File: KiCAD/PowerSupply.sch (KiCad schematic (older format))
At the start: 12 parts, among them J4 USB-Micro, Q1 3.7A, 30V, U2 LM1117-5.0, U3 AP2112K-3.3

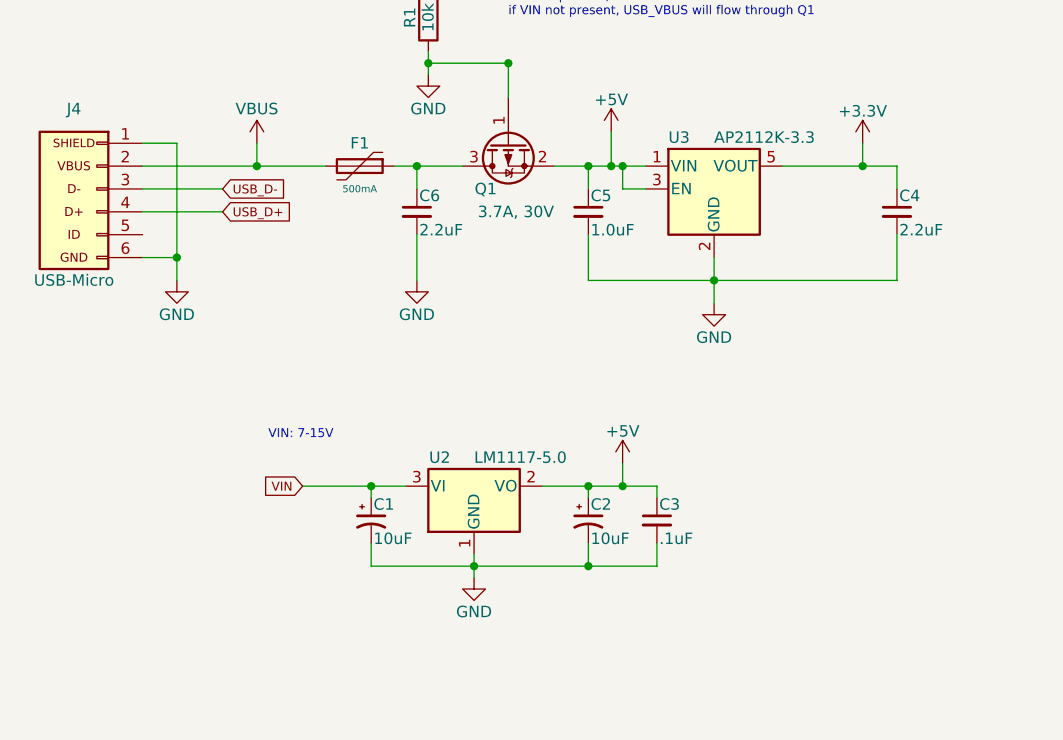
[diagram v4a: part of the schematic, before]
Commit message: Board layout and fixing schematic errors
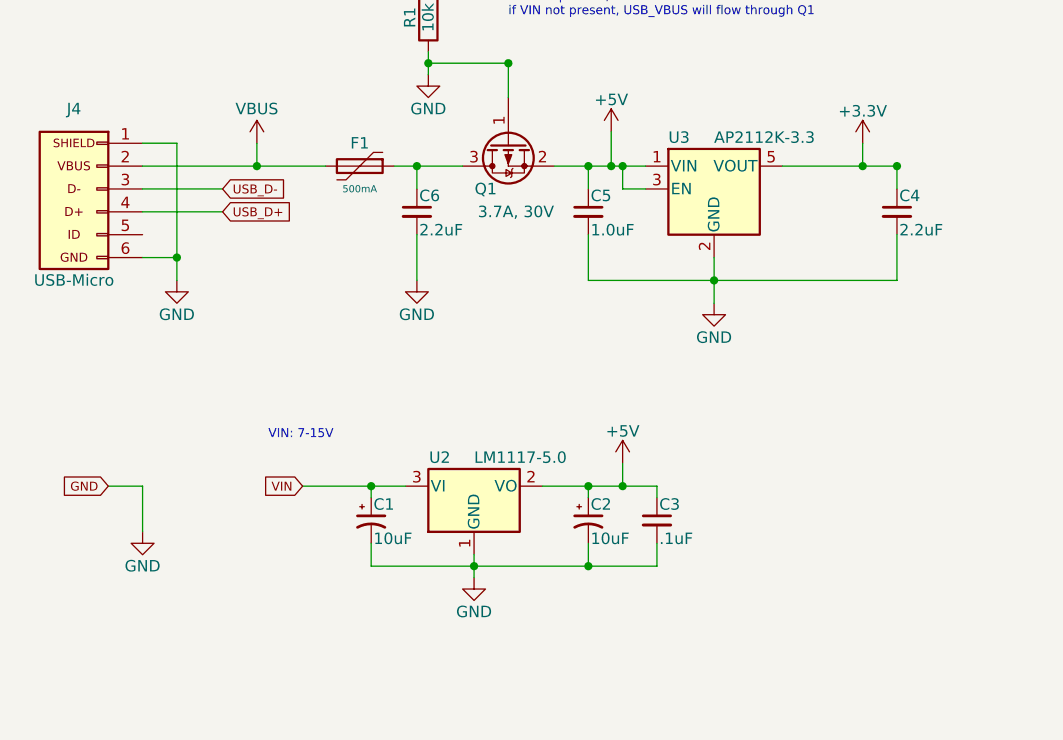
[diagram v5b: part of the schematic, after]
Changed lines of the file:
@@
 $EndDescr
 $Comp
-L GND #PWR027
+L GND #PWR025
 U 1 1 5BF271E8
 P 4600 3950
-F 0 "#PWR027" H 4600 3700 50  0001 C CNN
+F 0 "#PWR025" H 4600 3700 50  0001 C CNN
 F 1 "GND" H 4600 3800 50  0000 C CNN
 F 2 "" H 4600 3950 50  0001 C CNN
@@
 $EndComp
 $Comp
-L GND #PWR028
+L GND #PWR026
 U 1 1 5BF2720F
 P 5700 3050
-F 0 "#PWR028" H 5700 2800 50  0001 C CNN
+F 0 "#PWR026" H 5700 2800 50  0001 C CNN
 F 1 "GND" H 5700 2900 50  0000 C CNN
 F 2 "" H 5700 3050 50  0001 C CNN
@@
 VIN
 $Comp
-L +5V #PWR029
+L +5V #PWR027
 U 1 1 5BF27217
 P 5700 2600
-F 0 "#PWR029" H 5700 2450 50  0001 C CNN
+F 0 "#PWR027" H 5700 2450 50  0001 C CNN
 F 1 "+5V" H 5700 2740 50  0000 C CNN
 F 2 "" H 5700 2600 50  0001 C CNN
@@
 VIN: 7-15V
 $Comp
-L GND #PWR030
+L GND #PWR028
 U 1 1 5BF27ED3
 P 5900 5250
-F 0 "#PWR030" H 5900 5000 50  0001 C CNN
+F 0 "#PWR028" H 5900 5000 50  0001 C CNN
 F 1 "GND" H 5900 5100 50  0000 C CNN
 F 2 "" H 5900 5250 50  0001 C CNN
@@
 $EndComp
 $Comp
-L +5V #PWR031
+L +5V #PWR029
 U 1 1 5BF285D5
 P 6550 4750
-F 0 "#PWR031" H 6550 4600 50  0001 C CNN
+F 0 "#PWR029" H 6550 4600 50  0001 C CNN
 F 1 "+5V" H 6550 4890 50  0000 C CNN
 F 2 "" H 6550 4750 50  0001 C CNN
@@
 $EndComp
 $Comp
-L GND #PWR032
+L GND #PWR030
 U 1 1 5BF28EA0
 P 6950 4050
-F 0 "#PWR032" H 6950 3800 50  0001 C CNN
+F 0 "#PWR030" H 6950 3800 50  0001 C CNN
 F 1 "GND" H 6950 3900 50  0000 C CNN
 F 2 "" H 6950 4050 50  0001 C CNN
@@
 $EndComp
 $Comp
-L +3.3V #PWR033
+L +3.3V #PWR031
 U 1 1 5BF2913F
 P 7600 3350
-F 0 "#PWR033" H 7600 3200 50  0001 C CNN
+F 0 "#PWR031" H 7600 3200 50  0001 C CNN
 F 1 "+3.3V" H 7600 3490 50  0000 C CNN
 F 2 "" H 7600 3350 50  0001 C CNN
@@
 $EndComp
 $Comp
-L GND #PWR034
+L GND #PWR032
 U 1 1 5BF29400
 P 5650 3950
-F 0 "#PWR034" H 5650 3700 50  0001 C CNN
+F 0 "#PWR032" H 5650 3700 50  0001 C CNN
 F 1 "GND" H 5650 3800 50  0000 C CNN
 F 2 "" H 5650 3950 50  0001 C CNN
@@
 $EndComp
 $Comp
-L +5V #PWR035
+L +5V #PWR033
 U 1 1 5BF2A2B6
 P 6500 3300
-F 0 "#PWR035" H 6500 3150 50  0001 C CNN
+F 0 "#PWR033" H 6500 3150 50  0001 C CNN
 F 1 "+5V" H 6500 3440 50  0000 C CNN
 F 2 "" H 6500 3300 50  0001 C CNN
@@
 If VIN is present, MOSFET will not conduct\nif VIN not present, USB_VBUS will flow through Q1
 $Comp
-L VBUS #PWR036
+L VBUS #PWR034
 U 1 1 5BF2FD1D
 P 4950 3350
-F 0 "#PWR036" H 4950 3200 50  0001 C CNN
+F 0 "#PWR034" H 4950 3200 50  0001 C CNN
 F 1 "VBUS" H 4950 3500 50  0000 C CNN
 F 2 "" H 4950 3350 50  0001 C CNN
@@
 Wire Wire Line
 	6950 3850 6950 4050
-Wire Wire Line
-	7250 3450 7750 3450
 Connection ~ 6550 4850
 Wire Wire Line
@@
 Text Notes 7000 7100 0    79   ~ 0
 Author: Matthew Cox\nOrganization: University of Connecticut Formula SAE
+Text GLabel 4300 4850 0    39   Input ~ 0
+GND
+$Comp
+L GND #PWR035
+U 1 1 5C0C06A6
+P 4450 5050
+F 0 "#PWR035" H 4450 4800 50  0001 C CNN
+F 1 "GND" H 4450 4900 50  0000 C CNN
+F 2 "" H 4450 5050 50  0001 C CNN
+F 3 "" H 4450 5050 50  0001 C CNN
+	1    4450 5050
+	1    0    0    -1
+$EndComp
+Wire Wire Line
+	4300 4850 4450 4850
+Wire Wire Line
+	4450 4850 4450 5050
+Connection ~ 7750 3450
+Wire Wire Line
+	7250 3450 7750 3450
 $EndSCHEMATC

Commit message: Place and route
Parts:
- removed U2: LM1117-5.0, TO_SOT_Packages_SMD:SOT-223, symbol LM1117-5.0
- added U2: LM1117, TO_SOT_Packages_SMD:SOT-223, symbol LM1117
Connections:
- net +5V: now also U2.2 (VO), U2.4 (VO)
- net GND: now also U2.1 (GND)
- net VIN: now also U2.3 (VI)
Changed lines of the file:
@@
 LIBS:cortex_debug
 LIBS:B3FS-4005P
+LIBS:lm1117_edited
 LIBS:SAMD21-DevBoard-cache
 EELAYER 25 0
@@
 	1    0    0    -1
 $EndComp
-$Comp
-L LM1117-5.0 U2
-U 1 1 5BF2791A
-P 5900 4850
-F 0 "U2" H 5750 4975 50  0000 C CNN
-F 1 "LM1117-5.0" H 5900 4975 50  0000 L CNN
-F 2 "TO_SOT_Packages_SMD:SOT-223" H 5900 4850 50  0001 C CNN
-F 3 "" H 5900 4850 50  0001 C CNN
-	1    5900 4850
-	1    0    0    -1
-$EndComp
 Text Notes 5000 4650 0    39   ~ 0
 VIN: 7-15V
@@
 Wire Wire Line
 	7250 3450 7750 3450
+$Comp
+L LM1117 U2
+U 1 1 5C0C6154
+P 5900 4850
+F 0 "U2" H 5750 4975 50  0000 C CNN
+F 1 "LM1117" H 5900 4975 50  0000 L CNN
+F 2 "TO_SOT_Packages_SMD:SOT-223" H 5900 4850 50  0001 C CNN
+F 3 "" H 5900 4850 50  0001 C CNN
+	1    5900 4850
+	1    0    0    -1
+$EndComp
+Wire Wire Line
+	6200 4950 6250 4950
+Wire Wire Line
+	6250 4950 6250 4850
+Connection ~ 6250 4850
 $EndSCHEMATC

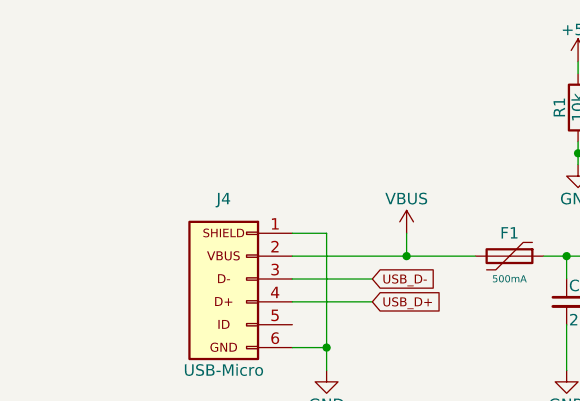
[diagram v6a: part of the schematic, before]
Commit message: Revising layout with different board outline
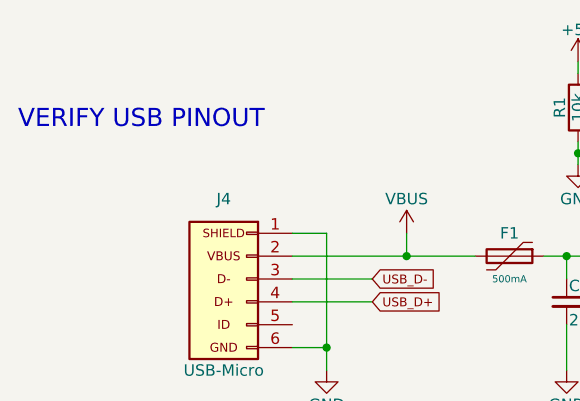
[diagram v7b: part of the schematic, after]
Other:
- note added: "VERIFY USB PINOUT"
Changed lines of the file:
@@
 LIBS:B3FS-4005P
 LIBS:lm1117_edited
+LIBS:fsmcttr
 LIBS:SAMD21-DevBoard-cache
 EELAYER 25 0
@@
 	6250 4950 6250 4850
 Connection ~ 6250 4850
+Text Notes 3250 2900 0    79   ~ 0
+VERIFY USB PINOUT
 $EndSCHEMATC

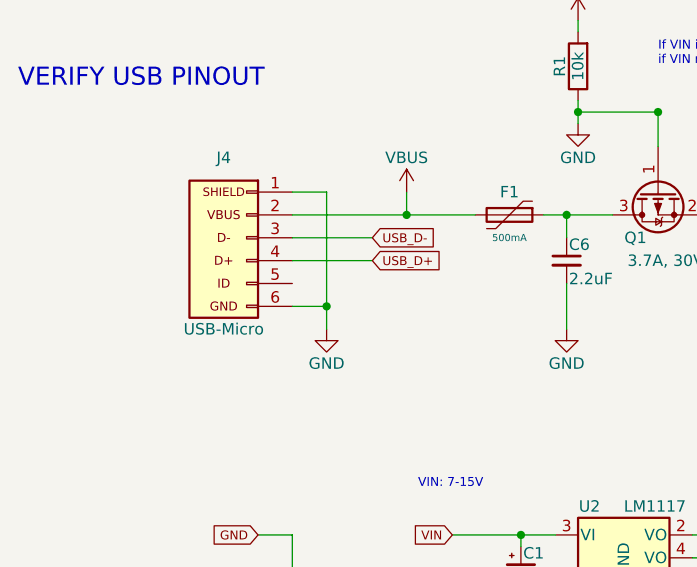
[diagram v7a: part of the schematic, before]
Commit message: Finished routing, now fine tweaking and tuning
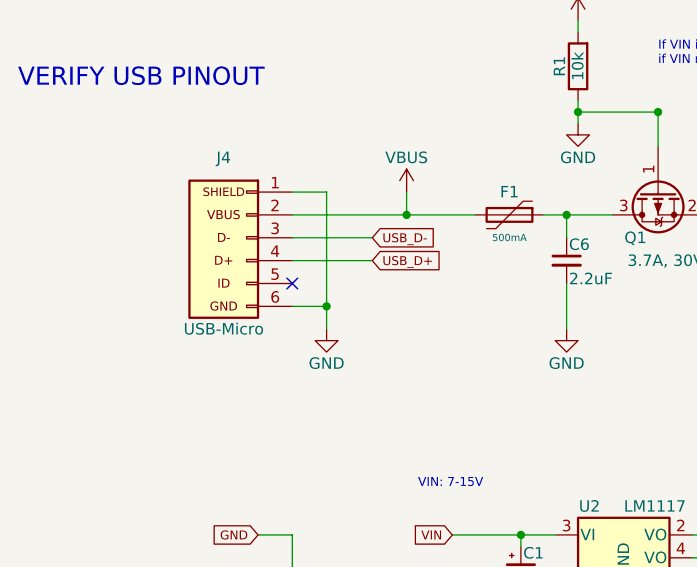
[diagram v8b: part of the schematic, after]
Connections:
- no-connect marks 0 -> 1
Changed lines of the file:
@@
 Text Notes 3250 2900 0    79   ~ 0
 VERIFY USB PINOUT
+NoConn ~ 4450 3750
 $EndSCHEMATC
